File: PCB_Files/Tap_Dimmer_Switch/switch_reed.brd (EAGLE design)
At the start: 91.2 x 90.7 mm, 37 parts, among them P1 HT7333

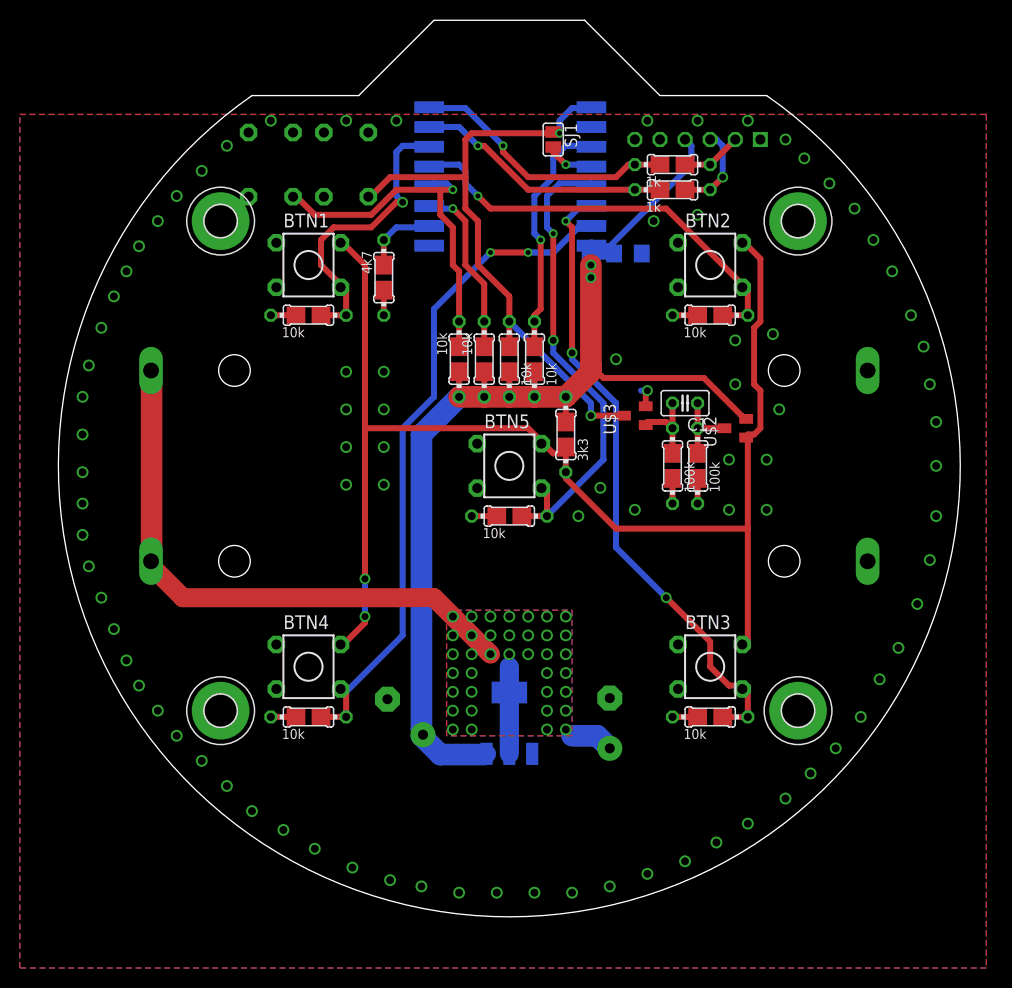
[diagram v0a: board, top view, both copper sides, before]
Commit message: Added Design with additional reed (magnet) sensor
this version is not entirely finished and has to be improved upon
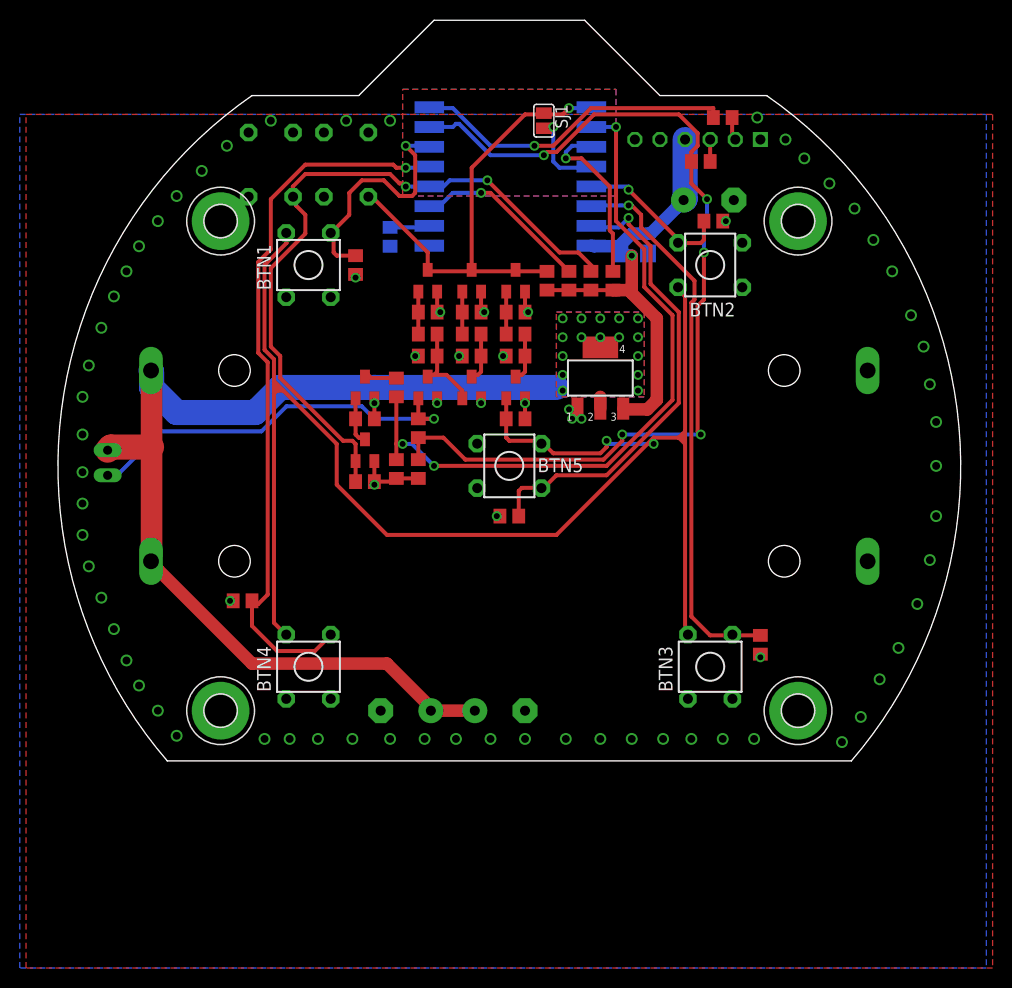
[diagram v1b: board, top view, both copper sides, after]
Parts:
- added C4, C6: 10nF, rcl:C0805
- added C7: 100u, rcl:E5-8,5
- added R16, R17, R18, R19, R20, R22, R23, R25: 200k, rcl:R0805
- added R21: 100k, rcl:R0805
- added R24: 50k, rcl:R0805
- added REED: (no value), jumper:JP1
- added U$1, U$5, U$7: AO3401, diyHue:SOT23
- added U$4, U$6, U$8: IRLML2502, diyHue:SOT23
- C1: device rcl:C025-025X050 -> rcl:C0805
- C2, C3: value 10nF -> 100u
- C5: value 100u -> 10u
- R1, R11, R12, R13, R14, R15, R2, R3, R4, R5, R8, R9: device diyHue:MULTI_RESISTOR -> rcl:R0805
- R10: value 4k7 -> 10k; device diyHue:MULTI_RESISTOR -> rcl:R0805
- R6, R7: value 100k -> 200k; device diyHue:MULTI_RESISTOR -> rcl:R0805
- moved C2 60.6 mm to (20.2, 26.9), turned to 180 degrees
- moved P1 36.1 mm to (9.21, 8.89), flipped to the top
- moved U$2 22.6 mm to (0.64, 7.94), turned to 0 degrees
- moved R7 22.2 mm to (0.64, 15.6), turned to 180 degrees
- moved R6 21.5 mm to (0.64, 11.1), turned to 0 degrees
- moved C3 20.7 mm to (-10.5, -24.8), turned to 0 degrees
- moved C1 18.5 mm to (0.64, 13.3)
- moved U$3 18.2 mm to (0.64, 18.7), turned to 0 degrees
- moved R12 15.5 mm to (8.26, 18.7)
- moved R5 13.5 mm to (-27.0, -13.7)
- moved R11 11.7 mm to (6.03, 18.7)
- moved R9 11.2 mm to (10.5, 18.7)
- moved R3 9.53 mm to (20.6, 24.8), turned to 180 degrees
- moved R4 8.90 mm to (25.4, -18.1), turned to 90 degrees
- moved R8 8.80 mm to (3.81, 18.7)
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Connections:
- removed net N$9: R15.1@1, R15.1@2, U2.RXD0
- new net ADC: R23.1, R24.2, U2.ADC
- new net ESP_RX: R15.1, R21.1, R25.2, U2.RXD0
- new net N$11: C6.1, R19.2, U$1.3, U$5.1
- new net N$12: C4.1, R16.2, U$5.3
- new net N$13: C4.2, R17.2, U$4.1
- new net N$14: C6.2, R18.2, U$6.1
- new net N$16: R20.2, U$7.1, U$8.3
- new net N$17: R23.2, U$7.3
- new net N$18: R21.2, REED.1, U$1.1
- net +3V3: now also R11.2, R12.2, R8.1, R9.1; no longer R1.2@1, R1.2@2, R11.2@1, R11.2@2, R12.2@1, R12.2@2, R8.1@1, R8.1@2, R9.1@1, R9.1@2, U$2.2
- net +5V: now also C7.+, R1.2, R20.1, REED.2, U$1.2, U$2.2, U$5.2, U$7.2
- net GND: now also C7.-, R10.2, R13.1, R16.1, R17.1, R18.1, R19.1, R2.1, R22.1, R24.1, R25.1, R3.1, R4.1, R5.1, R6.1, R7.1, U$4.2, U$6.2, U$8.2; no longer R10.2@1, R10.2@2, R13.1@1, R13.1@2, R2.1@1, R2.1@2, R3.1@1, R3.1@2, R4.1@1, R4.1@2, R5.1@1, R5.1@2, R6.1@1, R6.1@2, R7.1@1, R7.1@2
- net GP0: now also R12.1, R22.2, U$8.1; no longer R12.1@1, R12.1@2
- net GP12: now also R4.2; no longer R4.2@1, R4.2@2
- net GP13: now also BTN5.D, R13.2; no longer BTN4.D, R5.2@1, R5.2@2
- net GP14: now also BTN2.D, R3.2; no longer BTN5.D, R13.2@1, R13.2@2
- net GP4: now also R2.2; no longer R2.2@1, R2.2@2
- net GP5: now also BTN4.D, R5.2; no longer BTN2.D, R3.2@1, R3.2@2
- net N$2: now also R9.2; no longer R9.2@1, R9.2@2
- net N$3: now also R7.2; no longer R7.2@1, R7.2@2
- net N$4: now also R10.1; no longer R10.1@1, R10.1@2
- net N$5: now also R11.1; no longer R11.1@1, R11.1@2
- net N$6: now also R14.1; no longer R14.1@1, R14.1@2
- net N$7: now also R6.2; no longer R6.2@1, R6.2@2
- net N$8: now also R1.1; no longer R1.1@1, R1.1@2
- net RST: now also R8.2, U$4.3, U$6.3; no longer R8.2@1, R8.2@2
- net RX: now also R14.2; no longer R14.2@1, R14.2@2
- net TX: now also R15.2; no longer R15.2@1, R15.2@2
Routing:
- net ESP_RX: track 0.00 -> 97.1 mm, vias 0 -> 5
- net +3V3: track 123.6 -> 48.1 mm, vias 2 -> 1
- net ADC: track 0.00 -> 72.2 mm, vias 0 -> 3
- net +5V: track 70.9 -> 121.2 mm, vias 37 -> 20
- net N$18: track 0.00 -> 40.1 mm, vias 0 -> 1
- net GP0: track 37.4 -> 72.5 mm, vias 1 -> 2
- net GP14: track 48.1 -> 16.2 mm, vias 2 -> 1
- net GP5: track 43.4 -> 73.6 mm
- net N$8: track 131.3 -> 158.1 mm
- net N$9: track 26.0 -> 0.00 mm, vias 1 -> 0
- net GP13: track 69.5 -> 47.5 mm, vias 2 -> 1
- net RST: track 64.7 -> 47.8 mm, vias 2 -> 1
- net N$11: track 0.00 -> 9.37 mm
- net GP12: track 64.5 -> 56.3 mm, vias 3 -> 1
- net N$2: track 24.8 -> 17.9 mm
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- added copper zone on layer 1, net N$10
- added copper zone on layer 16, net N$10
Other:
- board size 91.2 x 90.7 mm -> 91.3 x 74.9 mm

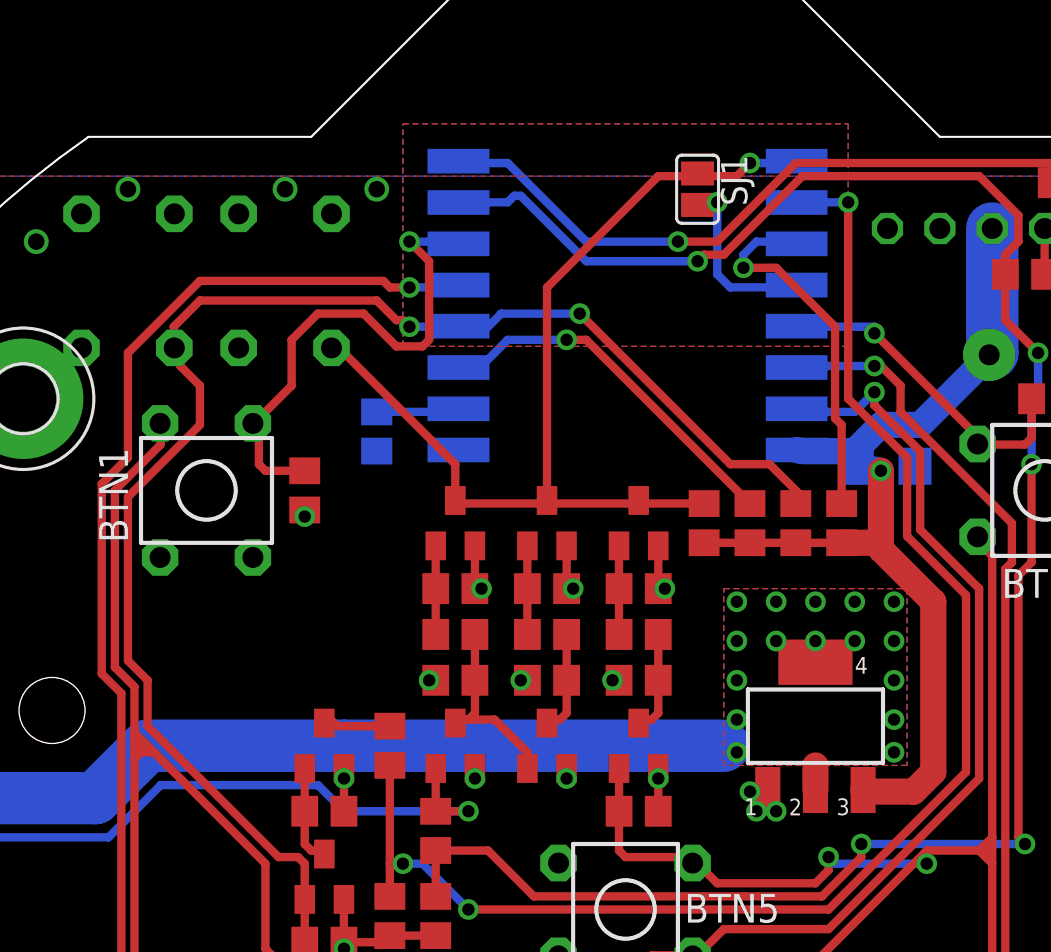
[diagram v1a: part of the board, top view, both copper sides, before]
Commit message: created additional compact design of ws2812b module
this new design features smaller footprint, but the esp module ist partially outside the board, which will result in better wifi connection.

additionally the footprint of the HT7333 has been fixed as previously it had used the wrong package.
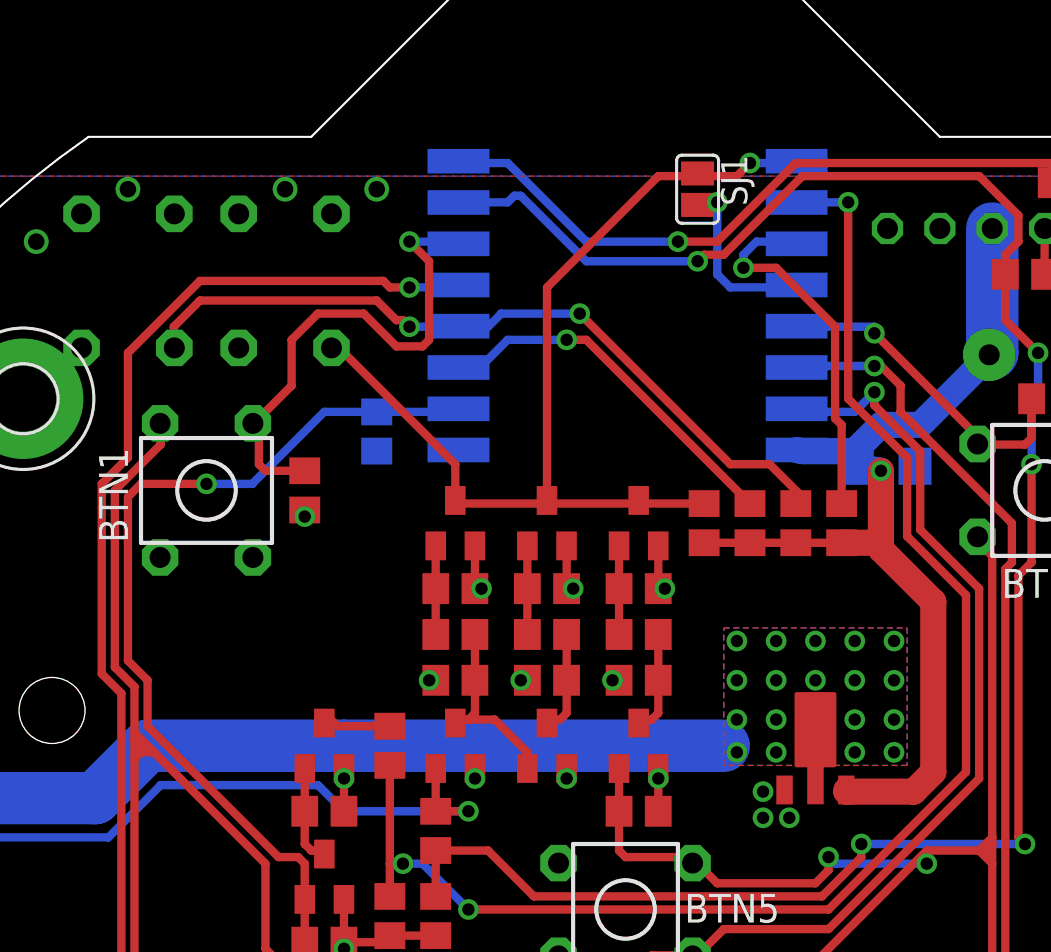
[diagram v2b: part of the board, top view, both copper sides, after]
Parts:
- P1: device diyHue:SOT223 -> diyHue:SOT89
- moved P1 1.11 mm to (9.21, 7.78)
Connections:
- removed net N$4: R10.1, U2.GPIO15
- new net GP15: R10.1, R22.2, U$8.1, U2.GPIO15
- net +5V: now also P1.2@1; no longer P1.4
- net GP0: no longer R22.2, U$8.1
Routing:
- net GP15: track 0.00 -> 44.0 mm, vias 0 -> 1
- net GP0: track 72.5 -> 37.6 mm
- net GND: track 24.7 -> 19.4 mm
- net N$4: track 4.53 -> 0.00 mm
- net +5V: track 121.2 -> 120.0 mm, vias 20 -> 22
- net +3V3: track 48.1 -> 48.9 mm
- removed copper zone on layer 1, net N$10
- removed copper zone on layer 16, net N$10
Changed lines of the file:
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@@
 </element>
 <element name="C1" library="rcl" package="C0805" value="10nF" x="0.635" y="13.335" smashed="yes" rot="R180"/>
-<element name="P1" library="diyHue" package="SOT223" value="HT7333" x="9.2075" y="8.89" smashed="yes">
-<attribute name="VALUE" x="14.9733" y="5.3975" size="1.27" layer="27" rot="R90"/>
+<element name="P1" library="diyHue" package="SOT89" value="HT7333" x="9.2075" y="7.775575" smashed="yes">
+<attribute name="VALUE" x="15.2908" y="6.505575" size="1.27" layer="27" rot="R90"/>
 </element>
 <element name="FTDI" library="pinhead-2" package="1X06-S" value="" x="19.05" y="33.02" smashed="yes" rot="MR0">
@@
 <wire x1="-27.9375" y1="-13.6525" x2="-28.2575" y2="-13.6525" width="0.4064" layer="1"/>
 <via x="-28.2575" y="-13.6525" extent="1-16" drill="0.6"/>
-<wire x1="6.8961" y1="5.7912" x2="6.8961" y2="5.1689" width="0.4064" layer="1"/>
-<wire x1="6.8961" y1="5.1689" x2="7.3025" y2="4.7625" width="0.4064" layer="1"/>
-<via x="7.3025" y="4.7625" extent="1-16" drill="0.6"/>
-<wire x1="7.3025" y1="4.7625" x2="6.35" y2="4.7625" width="0.4064" layer="16"/>
-<via x="6.35" y="4.7625" extent="1-16" drill="0.6"/>
-<wire x1="6.35" y1="4.7625" x2="6.35" y2="5.08" width="0.4064" layer="1"/>
-<wire x1="6.35" y1="5.08" x2="6.985" y2="5.715" width="0.4064" layer="1"/>
-<wire x1="6.985" y1="5.715" x2="6.0325" y2="5.715" width="0.4064" layer="1"/>
-<via x="6.0325" y="5.715" extent="1-16" drill="0.6"/>
-<wire x1="6.0325" y1="5.715" x2="6.985" y2="5.715" width="0.4064" layer="16"/>
+<via x="7.9375" y="4.445" extent="1-16" drill="0.6"/>
+<via x="6.6675" y="4.445" extent="1-16" drill="0.6"/>
+<via x="6.6675" y="5.715" extent="1-16" drill="0.6"/>
 <wire x1="-7.3025" y1="15.5575" x2="-7.3025" y2="17.4625" width="0.4064" layer="1"/>
 <wire x1="-7.3025" y1="17.4625" x2="-7.305" y2="17.6325" width="0.4064" layer="1"/>
@@
 <contactref element="P1" pad="2"/>
 <contactref element="C3" pad="+"/>
-<contactref element="P1" pad="4"/>
+<contactref element="P1" pad="2@1"/>
 <wire x1="-36.195" y1="9.525" x2="-36.195" y2="1.905" width="2.1844" layer="1"/>
 <wire x1="-36.195" y1="1.905" x2="-36.195" y2="-8.89" width="2.1844" layer="1"/>
@@
 <vertex x="13.6525" y="6.985"/>
 <vertex x="4.7625" y="6.985"/>
-<vertex x="4.7625" y="15.5575"/>
-<vertex x="13.6525" y="15.5575"/>
+<vertex x="4.7625" y="13.6525"/>
+<vertex x="13.6525" y="13.6525"/>
 </polygon>
 <polygon width="0.4064" layer="1" thermals="no">
 <vertex x="13.6525" y="6.985"/>
 <vertex x="4.7625" y="6.985"/>
-<vertex x="4.7625" y="15.5575"/>
-<vertex x="13.6525" y="15.5575"/>
+<vertex x="4.7625" y="13.6525"/>
+<vertex x="13.6525" y="13.6525"/>
 </polygon>
-<via x="5.3975" y="14.9225" extent="1-16" drill="0.6"/>
-<via x="7.3025" y="14.9225" extent="1-16" drill="0.6"/>
-<via x="9.2075" y="14.9225" extent="1-16" drill="0.6"/>
-<via x="11.1125" y="14.9225" extent="1-16" drill="0.6"/>
+<via x="7.3025" y="13.0175" extent="1-16" drill="0.6"/>
+<via x="7.3025" y="11.1125" extent="1-16" drill="0.6"/>
+<via x="11.1125" y="9.2075" extent="1-16" drill="0.6"/>
+<via x="11.1125" y="7.62" extent="1-16" drill="0.6"/>
 <via x="13.0175" y="13.0175" extent="1-16" drill="0.6"/>
 <via x="13.0175" y="11.1125" extent="1-16" drill="0.6"/>
@@
 <via x="5.3975" y="9.2075" extent="1-16" drill="0.6"/>
 <via x="5.3975" y="7.62" extent="1-16" drill="0.6"/>
-<via x="7.3025" y="13.0175" extent="1-16" drill="0.6"/>
-<via x="11.1125" y="13.0175" extent="1-16" drill="0.6"/>
-<via x="9.2075" y="13.0175" extent="1-16" drill="0.6"/>
-<wire x1="9.2075" y1="5.7912" x2="9.2075" y2="6.985" width="1.27" layer="1"/>
+<via x="7.3025" y="9.2075" extent="1-16" drill="0.6"/>
+<via x="11.1125" y="11.1125" extent="1-16" drill="0.6"/>
+<via x="9.2075" y="11.1125" extent="1-16" drill="0.6"/>
 <wire x1="-40.3225" y1="1.905" x2="-36.195" y2="1.905" width="2.54" layer="1"/>
 <wire x1="-40.64" y1="1.5875" x2="-40.3225" y2="1.905" width="2.54" layer="1"/>
@@
 <wire x1="-7.9375" y1="-24.4475" x2="-12.3825" y2="-20.0025" width="1.27" layer="1"/>
 <wire x1="-7.9375" y1="-24.4475" x2="-7.9375" y2="-24.765" width="1.27" layer="1"/>
-<via x="13.0175" y="14.9225" extent="1-16" drill="0.6"/>
+<via x="7.3025" y="7.62" extent="1-16" drill="0.6"/>
+<via x="9.2075" y="13.0175" extent="1-16" drill="0.6"/>
+<via x="11.1125" y="13.0175" extent="1-16" drill="0.6"/>
 </signal>
 <signal name="RST">
@@
 <wire x1="14.9225" y1="14.9225" x2="12.3825" y2="17.4625" width="1.27" layer="1"/>
 <wire x1="13.97" y1="5.715" x2="14.9225" y2="6.6675" width="1.27" layer="1"/>
-<wire x1="11.7475" y1="5.715" x2="13.97" y2="5.715" width="1.27" layer="1"/>
-<wire x1="11.7475" y1="5.715" x2="11.5189" y2="5.7912" width="1.27" layer="1"/>
 <wire x1="10.795" y1="17.78" x2="12.3825" y2="17.78" width="1.27" layer="1"/>
 <wire x1="12.3825" y1="17.78" x2="12.3825" y2="17.4625" width="1.27" layer="1"/>
@@
 <via x="12.3825" y="21.2725" extent="1-16" drill="0.6"/>
 <wire x1="12.3825" y1="21.2725" x2="12.3825" y2="17.78" width="1.27" layer="1"/>
-</signal>
-<signal name="N$4">
+<wire x1="13.97" y1="5.715" x2="10.7065" y2="5.715" width="1.27" layer="1"/>
+<wire x1="10.7065" y1="5.715" x2="10.7065" y2="5.794575" width="1.27" layer="1"/>
+</signal>
+<signal name="GP15">
 <contactref element="U2" pad="GPIO15"/>
 <contactref element="R10" pad="1"/>
@@
 <wire x1="-8.255" y1="24.13" x2="-8.1" y2="24.28" width="0.4064" layer="16"/>
 <wire x1="-11.43" y1="24.13" x2="-12.065" y2="24.1275" width="0.4064" layer="16"/>
+<contactref element="U$8" pad="1"/>
+<contactref element="R22" pad="2"/>
+<wire x1="-15.5575" y1="-1.5875" x2="-15.5575" y2="0.3175" width="0.4064" layer="1"/>
+<wire x1="-15.5575" y1="0.3175" x2="-15.555" y2="0.4875" width="0.4064" layer="1"/>
+<wire x1="-15.5575" y1="-1.5875" x2="-15.555" y2="-1.5875" width="0.4064" layer="1"/>
+<wire x1="-23.1775" y1="11.1125" x2="-24.13" y2="12.065" width="0.4064" layer="1"/>
+<wire x1="-23.1775" y1="8.89" x2="-23.1775" y2="11.1125" width="0.4064" layer="1"/>
+<wire x1="-16.8275" y1="2.54" x2="-23.1775" y2="8.89" width="0.4064" layer="1"/>
+<wire x1="-15.875" y1="2.54" x2="-16.8275" y2="2.54" width="0.4064" layer="1"/>
+<wire x1="-15.5575" y1="2.2225" x2="-15.875" y2="2.54" width="0.4064" layer="1"/>
+<wire x1="-15.5575" y1="0.635" x2="-15.5575" y2="2.2225" width="0.4064" layer="1"/>
+<wire x1="-15.5575" y1="0.635" x2="-15.555" y2="0.4875" width="0.4064" layer="1"/>
+<wire x1="-24.13" y1="20.0025" x2="-23.495" y2="20.6375" width="0.4064" layer="1"/>
+<wire x1="-24.13" y1="12.065" x2="-24.13" y2="20.0025" width="0.4064" layer="1"/>
+<wire x1="-14.605" y1="24.13" x2="-12.065" y2="24.13" width="0.4064" layer="16"/>
+<wire x1="-18.0975" y1="20.6375" x2="-14.605" y2="24.13" width="0.4064" layer="16"/>
+<wire x1="-20.32" y1="20.6375" x2="-18.0975" y2="20.6375" width="0.4064" layer="16"/>
+<wire x1="-23.495" y1="20.6375" x2="-20.32" y2="20.6375" width="0.4064" layer="1"/>
+<wire x1="-12.065" y1="24.13" x2="-12.065" y2="24.1275" width="0.4064" layer="16"/>
+<via x="-20.32" y="20.6375" extent="1-16" drill="0.6"/>
 </signal>
 <signal name="N$5">
@@
 <contactref element="U2" pad="GPIO0"/>
 <contactref element="GP0_BTN" pad="A"/>
-<contactref element="U$8" pad="1"/>
-<contactref element="R22" pad="2"/>
-<wire x1="-15.5575" y1="-1.5875" x2="-15.5575" y2="0.3175" width="0.4064" layer="1"/>
-<wire x1="-15.5575" y1="0.3175" x2="-15.555" y2="0.4875" width="0.4064" layer="1"/>
-<wire x1="-15.5575" y1="-1.5875" x2="-15.555" y2="-1.5875" width="0.4064" layer="1"/>
 <wire x1="-8.255" y1="28.2575" x2="-10.4775" y2="28.2575" width="0.4064" layer="16"/>
 <wire x1="-8.255" y1="28.2575" x2="-8.1" y2="28.28" width="0.4064" layer="16"/>
@@
 <wire x1="-21.9075" y1="27.305" x2="-21.9075" y2="28.2575" width="0.4064" layer="1"/>
 <wire x1="-21.9075" y1="27.305" x2="-21.88" y2="27.23" width="0.4064" layer="1"/>
-<wire x1="-15.875" y1="2.54" x2="-16.8275" y2="2.54" width="0.4064" layer="1"/>
-<wire x1="-15.5575" y1="2.2225" x2="-15.875" y2="2.54" width="0.4064" layer="1"/>
-<wire x1="-15.5575" y1="0.635" x2="-15.5575" y2="2.2225" width="0.4064" layer="1"/>
-<wire x1="-15.5575" y1="0.635" x2="-15.555" y2="0.4875" width="0.4064" layer="1"/>
-<wire x1="-20.6375" y1="23.495" x2="-24.13" y2="20.0025" width="0.4064" layer="1"/>
-<wire x1="-20.6375" y1="25.4" x2="-20.6375" y2="23.495" width="0.4064" layer="1"/>
-<wire x1="-21.59" y1="26.3525" x2="-20.6375" y2="25.4" width="0.4064" layer="1"/>
-<wire x1="-21.59" y1="26.9875" x2="-21.59" y2="26.3525" width="0.4064" layer="1"/>
-<wire x1="-21.59" y1="26.9875" x2="-21.88" y2="27.23" width="0.4064" layer="1"/>
-<wire x1="-24.13" y1="12.065" x2="-24.13" y2="20.0025" width="0.4064" layer="1"/>
-<wire x1="-23.1775" y1="11.1125" x2="-24.13" y2="12.065" width="0.4064" layer="1"/>
-<wire x1="-23.1775" y1="8.89" x2="-23.1775" y2="11.1125" width="0.4064" layer="1"/>
-<wire x1="-16.8275" y1="2.54" x2="-23.1775" y2="8.89" width="0.4064" layer="1"/>
 </signal>
 <signal name="N$3">
@@
 <wire x1="-9.2075" y1="15.5575" x2="-9.205" y2="15.5575" width="0.4064" layer="1"/>
 </signal>
-<signal name="N$10">
-<polygon width="0.6096" layer="16" pour="cutout">
-<vertex x="-10.795" y="38.1"/>
-<vertex x="10.795" y="38.1"/>
-<vertex x="10.795" y="27.305"/>
-<vertex x="-10.795" y="27.305"/>
-</polygon>
-<polygon width="0.6096" layer="1" pour="cutout">
-<vertex x="-10.795" y="38.1"/>
-<vertex x="10.795" y="38.1"/>
-<vertex x="10.795" y="27.305"/>
-<vertex x="-10.795" y="27.305"/>
-</polygon>
-</signal>
 <signal name="N$16">
